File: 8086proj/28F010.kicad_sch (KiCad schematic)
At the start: 5 parts

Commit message: started sram
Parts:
- U3: value (none) -> 74LS138
- U4, U5, U6, U7: value (none) -> 28F010; footprint (none) -> 28F010
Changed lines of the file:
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@@
       (effects (font (size 1.27 1.27)) hide)
     )
-    (property "Value" "" (id 1) (at 204.47 85.09 0))
+    (property "Value" "GND" (id 1) (at 204.47 85.09 0))
     (property "Footprint" "" (id 2) (at 204.47 80.01 0)
       (effects (font (size 1.27 1.27)) hide)
@@
       (effects (font (size 1.27 1.27)) hide)
     )
-    (property "Value" "" (id 1) (at 265.43 109.22 0))
+    (property "Value" "+5V" (id 1) (at 265.43 109.22 0))
     (property "Footprint" "" (id 2) (at 265.43 114.3 0)
       (effects (font (size 1.27 1.27)) hide)
@@
       (effects (font (size 1.27 1.27)) hide)
     )
-    (property "Value" "" (id 1) (at 209.55 157.48 0))
+    (property "Value" "GND" (id 1) (at 209.55 157.48 0))
     (property "Footprint" "" (id 2) (at 209.55 152.4 0)
       (effects (font (size 1.27 1.27)) hide)
@@
       (effects (font (size 1.524 1.524)))
     )
-    (property "Value" "" (id 1) (at 161.29 35.56 0)
-      (effects (font (size 1.524 1.524)))
-    )
-    (property "Footprint" "" (id 2) (at 161.29 37.084 0)
+    (property "Value" "28F010" (id 1) (at 161.29 35.56 0)
+      (effects (font (size 1.524 1.524)))
+    )
+    (property "Footprint" "28F010" (id 2) (at 161.29 37.084 0)
       (effects (font (size 1.524 1.524)) hide)
     )
@@
       (effects (font (size 1.27 1.27)) hide)
     )
-    (property "Value" "" (id 1) (at 186.69 111.76 0))
+    (property "Value" "+5V" (id 1) (at 186.69 111.76 0))
     (property "Footprint" "" (id 2) (at 186.69 116.84 0)
       (effects (font (size 1.27 1.27)) hide)
@@
       (effects (font (size 1.27 1.27)) hide)
     )
-    (property "Value" "" (id 1) (at 265.43 36.83 0))
+    (property "Value" "+5V" (id 1) (at 265.43 36.83 0))
     (property "Footprint" "" (id 2) (at 265.43 41.91 0)
       (effects (font (size 1.27 1.27)) hide)
@@
       (effects (font (size 1.27 1.27)) hide)
     )
-    (property "Value" "" (id 1) (at 133.35 86.36 0))
+    (property "Value" "GND" (id 1) (at 133.35 86.36 0))
     (property "Footprint" "" (id 2) (at 133.35 81.28 0)
       (effects (font (size 1.27 1.27)) hide)
@@
       (effects (font (size 1.27 1.27)) hide)
     )
-    (property "Value" "" (id 1) (at 57.15 45.72 0)
+    (property "Value" "Earth" (id 1) (at 57.15 45.72 0)
       (effects (font (size 1.27 1.27)) hide)
     )
@@
     (in_bom yes) (on_board yes) (fields_autoplaced)
     (property "Reference" "U3" (id 0) (at 71.12 41.91 0))
-    (property "Value" "" (id 1) (at 71.12 44.45 0))
+    (property "Value" "74LS138" (id 1) (at 71.12 44.45 0))
     (property "Footprint" "" (id 2) (at 71.12 54.61 0)
       (effects (font (size 1.27 1.27)) hide)
@@
       (effects (font (size 1.27 1.27)) hide)
     )
-    (property "Value" "" (id 1) (at 130.81 160.02 0))
+    (property "Value" "GND" (id 1) (at 130.81 160.02 0))
     (property "Footprint" "" (id 2) (at 130.81 154.94 0)
       (effects (font (size 1.27 1.27)) hide)
@@
       (effects (font (size 1.524 1.524)))
     )
-    (property "Value" "" (id 1) (at 237.49 34.29 0)
-      (effects (font (size 1.524 1.524)))
-    )
-    (property "Footprint" "" (id 2) (at 237.49 35.814 0)
+    (property "Value" "28F010" (id 1) (at 237.49 34.29 0)
+      (effects (font (size 1.524 1.524)))
+    )
+    (property "Footprint" "28F010" (id 2) (at 237.49 35.814 0)
       (effects (font (size 1.524 1.524)) hide)
     )
@@
       (effects (font (size 1.27 1.27)) hide)
     )
-    (property "Value" "" (id 1) (at 189.23 38.1 0))
+    (property "Value" "+5V" (id 1) (at 189.23 38.1 0))
     (property "Footprint" "" (id 2) (at 189.23 43.18 0)
       (effects (font (size 1.27 1.27)) hide)
@@
       (effects (font (size 1.524 1.524)))
     )
-    (property "Value" "" (id 1) (at 237.49 106.68 0)
-      (effects (font (size 1.524 1.524)))
-    )
-    (property "Footprint" "" (id 2) (at 237.49 108.204 0)
+    (property "Value" "28F010" (id 1) (at 237.49 106.68 0)
+      (effects (font (size 1.524 1.524)))
+    )
+    (property "Footprint" "28F010" (id 2) (at 237.49 108.204 0)
       (effects (font (size 1.524 1.524)) hide)
     )
@@
       (effects (font (size 1.524 1.524)))
     )
-    (property "Value" "" (id 1) (at 158.75 109.22 0)
-      (effects (font (size 1.524 1.524)))
-    )
-    (property "Footprint" "" (id 2) (at 158.75 110.744 0)
+    (property "Value" "28F010" (id 1) (at 158.75 109.22 0)
+      (effects (font (size 1.524 1.524)))
+    )
+    (property "Footprint" "28F010" (id 2) (at 158.75 110.744 0)
       (effects (font (size 1.524 1.524)) hide)
     )

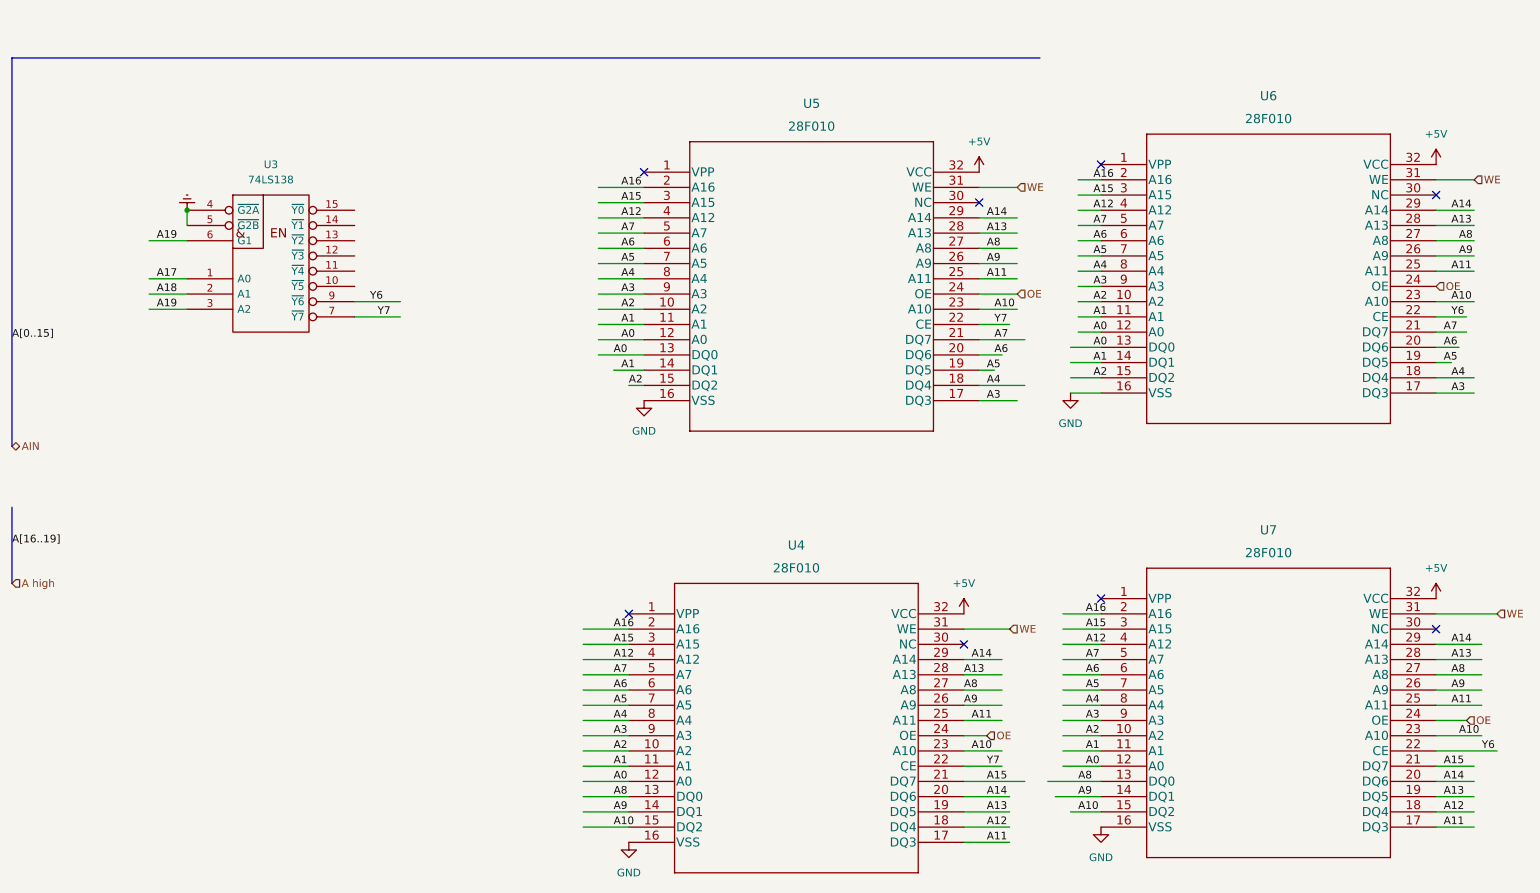
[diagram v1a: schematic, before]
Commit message: 28F010 fix
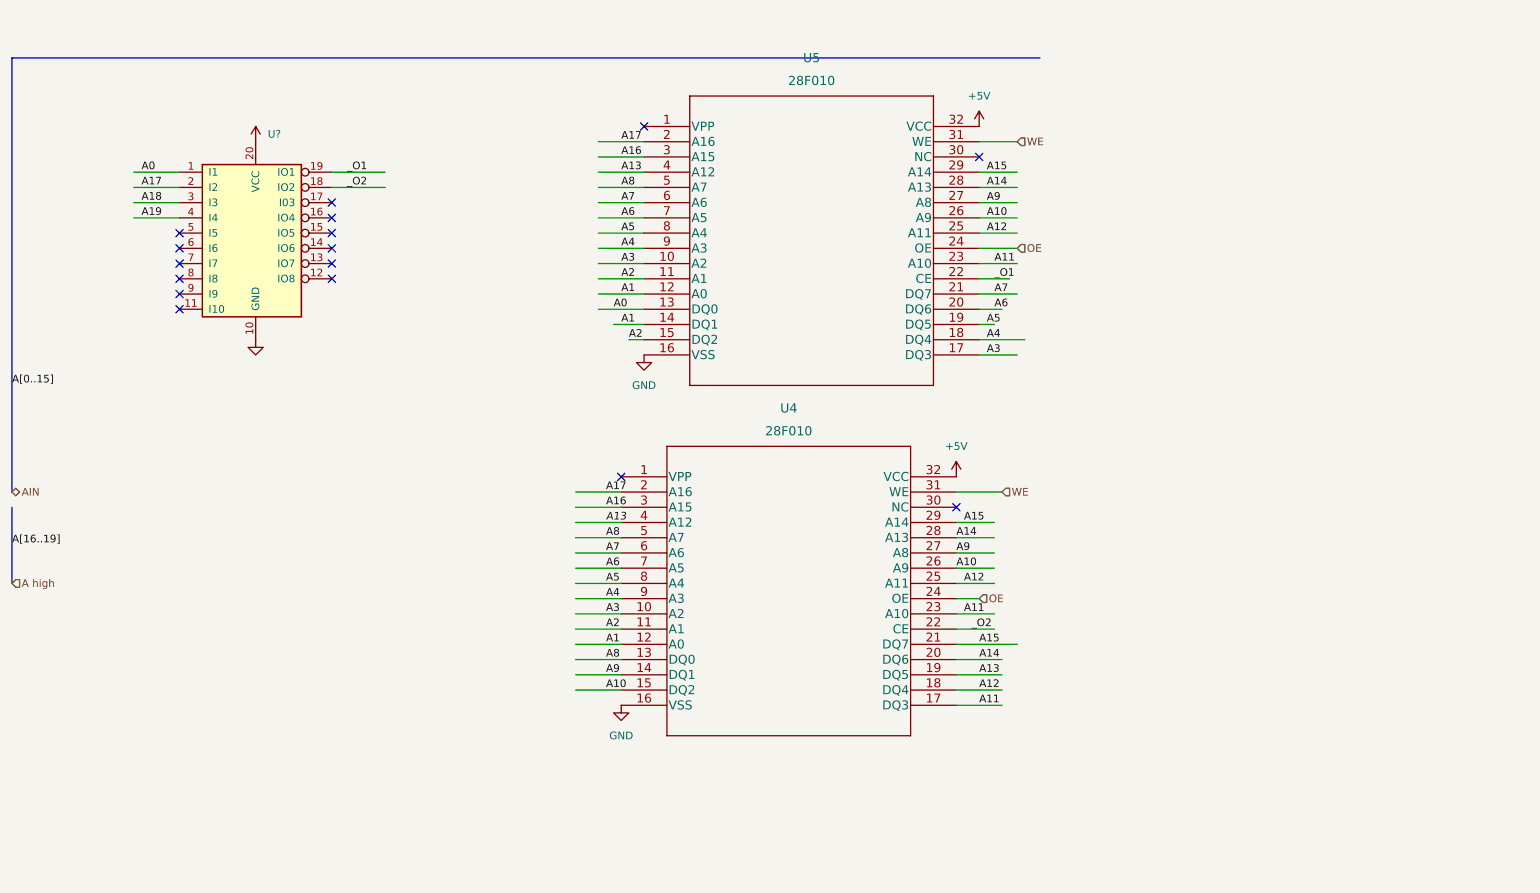
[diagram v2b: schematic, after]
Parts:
- removed U3: 74LS138, symbol 74xx_IEEE:74LS138
- removed U6, U7: 28F010, 28F010, symbol 28F010:28F010
- added U?: (no value), symbol Logic_Programmable:PAL16L8
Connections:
- net +5V: now also U?.20 (VCC)
- net A0: now also U?.1 (I1); no longer U4.12 (A0), U5.12 (A0)
- net A1: now also U4.12 (A0), U5.12 (A0); no longer U4.11 (A1), U5.11 (A1)
- net A10: now also U4.26 (A9), U5.26 (A9); no longer U4.23 (A10), U5.23 (A10)
- net A11: now also U4.23 (A10), U5.23 (A10); no longer U4.25 (A11), U5.25 (A11)
- net A12: now also U4.25 (A11), U5.25 (A11); no longer U4.4 (A12), U5.4 (A12)
- net A13: now also U4.4 (A12), U5.4 (A12); no longer U4.28 (A13), U5.28 (A13)
- net A14: now also U4.28 (A13), U5.28 (A13); no longer U4.29 (A14), U5.29 (A14)
- net A15: now also U4.29 (A14), U5.29 (A14); no longer U4.3 (A15), U5.3 (A15)
- net A16: now also U4.3 (A15), U5.3 (A15); no longer U4.2 (A16), U5.2 (A16)
- net A17: now also U4.2 (A16), U5.2 (A16), U?.2 (I2)
- net A18: now also U?.3 (I3)
- net A19: now also U?.4 (I4)
- net A2: now also U4.11 (A1), U5.11 (A1); no longer U4.10 (A2), U5.10 (A2)
- net A3: now also U4.10 (A2), U5.10 (A2); no longer U4.9 (A3), U5.9 (A3)
- net A4: now also U4.9 (A3), U5.9 (A3); no longer U4.8 (A4), U5.8 (A4)
- net A5: now also U4.8 (A4), U5.8 (A4); no longer U4.7 (A5), U5.7 (A5)
- net A6: now also U4.7 (A5), U5.7 (A5); no longer U4.6 (A6), U5.6 (A6)
- net A7: now also U4.6 (A6), U5.6 (A6); no longer U4.5 (A7), U5.5 (A7)
- net A8: now also U4.5 (A7), U5.5 (A7); no longer U4.27 (A8), U5.27 (A8)
- net A9: now also U4.27 (A8), U5.27 (A8); no longer U4.26 (A9), U5.26 (A9)
- net GND: now also U?.10 (GND)
- net Y7 renamed _O1
- net _O1: now also U?.19 (IO1); no longer U4.22 (CE)
- new net _O2: U4.22 (CE), U?.18 (IO2)
- no-connect marks 8 -> 16
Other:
- moved on the sheet: U4, U5

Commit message: latch added
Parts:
- U?: value (none) -> PAL16L8
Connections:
- net A0: no longer U5.13 (DQ0)
- net A1: no longer U5.14 (DQ1)
- net A10: no longer U4.15 (DQ2)
- net A11: no longer U4.17 (DQ3)
- net A12: no longer U4.18 (DQ4)
- net A13: no longer U4.19 (DQ5)
- net A14: no longer U4.20 (DQ6)
- net A15: no longer U4.21 (DQ7)
- net A2: no longer U5.15 (DQ2)
- net A3: no longer U5.17 (DQ3)
- net A4: no longer U5.18 (DQ4)
- net A5: no longer U5.19 (DQ5)
- net A6: no longer U5.20 (DQ6)
- net A7: no longer U5.21 (DQ7)
- net A8: no longer U4.13 (DQ0)
- net A9: no longer U4.14 (DQ1)
- new net D0: U5.13 (DQ0)
- new net D1: U5.14 (DQ1)
- new net D10: U4.15 (DQ2)
- new net D11: U4.17 (DQ3)
- new net D12: U4.18 (DQ4)
- new net D13: U4.19 (DQ5)
- new net D14: U4.20 (DQ6)
- new net D15: U4.21 (DQ7)
- new net D2: U5.15 (DQ2)
- new net D3: U5.17 (DQ3)
- new net D4: U5.18 (DQ4)
- new net D5: U5.19 (DQ5)
- new net D6: U5.20 (DQ6)
- new net D7: U5.21 (DQ7)
- new net D8: U4.13 (DQ0)
- new net D9: U4.14 (DQ1)
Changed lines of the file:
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@@
-    (stroke (width 0) (type default) (color 0 0 0 0))
-  )
-  (bus (pts (xy 27.94 99.06) (xy 27.94 111.76))
     (stroke (width 0) (type default) (color 0 0 0 0))
   )
@@
     (stroke (width 0) (type default) (color 0 0 0 0))
   )
+  (bus (pts (xy 27.94 109.22) (xy 27.94 130.81))
+    (stroke (width 0) (type default) (color 0 0 0 0))
+  )
   (wire (pts (xy 189.23 68.58) (xy 191.77 68.58))
     (stroke (width 0) (type default) (color 0 0 0 0))
@@
     (effects (font (size 1.27 1.27)) (justify left bottom))
   )
-  (label "A0" (at 128.27 66.04 0)
-    (effects (font (size 1.27 1.27)) (justify left bottom))
-  )
-  (label "A7" (at 191.77 63.5 0)
-    (effects (font (size 1.27 1.27)) (justify left bottom))
-  )
-  (label "A13" (at 189.23 127 0)
+  (label "D0" (at 128.27 66.04 0)
+    (effects (font (size 1.27 1.27)) (justify left bottom))
+  )
+  (label "D7" (at 191.77 63.5 0)
+    (effects (font (size 1.27 1.27)) (justify left bottom))
+  )
+  (label "D13" (at 189.23 127 0)
     (effects (font (size 1.27 1.27)) (justify left bottom))
   )
@@
     (effects (font (size 1.27 1.27)) (justify left bottom))
   )
-  (label "A2" (at 130.81 71.12 0)
-    (effects (font (size 1.27 1.27)) (justify left bottom))
-  )
-  (label "A5" (at 190.5 68.58 0)
+  (label "D2" (at 130.81 71.12 0)
+    (effects (font (size 1.27 1.27)) (justify left bottom))
+  )
+  (label "D5" (at 190.5 68.58 0)
     (effects (font (size 1.27 1.27)) (justify left bottom))
   )
@@
     (effects (font (size 1.27 1.27)) (justify left bottom))
   )
-  (label "A6" (at 191.77 66.04 0)
+  (label "D6" (at 191.77 66.04 0)
     (effects (font (size 1.27 1.27)) (justify left bottom))
   )
@@
     (effects (font (size 1.27 1.27)) (justify left bottom))
   )
-  (label "A9" (at 127 127 0)
-    (effects (font (size 1.27 1.27)) (justify left bottom))
-  )
-  (label "A1" (at 129.54 68.58 0)
+  (label "D9" (at 127 127 0)
+    (effects (font (size 1.27 1.27)) (justify left bottom))
+  )
+  (label "D1" (at 129.54 68.58 0)
     (effects (font (size 1.27 1.27)) (justify left bottom))
   )
@@
     (effects (font (size 1.27 1.27)) (justify left bottom))
   )
-  (label "A8" (at 127 124.46 0)
+  (label "D8" (at 127 124.46 0)
+    (effects (font (size 1.27 1.27)) (justify left bottom))
+  )
+  (label "D[0..15]" (at 27.94 119.38 0)
     (effects (font (size 1.27 1.27)) (justify left bottom))
   )
@@
     (effects (font (size 1.27 1.27)) (justify left bottom))
   )
-  (label "A10" (at 127 129.54 0)
+  (label "D10" (at 127 129.54 0)
     (effects (font (size 1.27 1.27)) (justify left bottom))
   )
@@
     (effects (font (size 1.27 1.27)) (justify left bottom))
   )
-  (label "A15" (at 189.23 121.92 0)
-    (effects (font (size 1.27 1.27)) (justify left bottom))
-  )
-  (label "A11" (at 189.23 132.08 0)
+  (label "D15" (at 189.23 121.92 0)
+    (effects (font (size 1.27 1.27)) (justify left bottom))
+  )
+  (label "D11" (at 189.23 132.08 0)
     (effects (font (size 1.27 1.27)) (justify left bottom))
   )
@@
     (effects (font (size 1.27 1.27)) (justify left bottom))
   )
-  (label "A[0..15]" (at 27.94 78.74 0)
+  (label "A[0..19]" (at 27.94 78.74 0)
     (effects (font (size 1.27 1.27)) (justify left bottom))
   )
@@
     (effects (font (size 1.27 1.27)) (justify left bottom))
   )
-  (label "A14" (at 189.23 124.46 0)
+  (label "D14" (at 189.23 124.46 0)
     (effects (font (size 1.27 1.27)) (justify left bottom))
   )
@@
     (effects (font (size 1.27 1.27)) (justify left bottom))
   )
-  (label "A4" (at 190.5 71.12 0)
+  (label "D4" (at 190.5 71.12 0)
     (effects (font (size 1.27 1.27)) (justify left bottom))
   )
@@
     (effects (font (size 1.27 1.27)) (justify left bottom))
   )
-  (label "A[16..19]" (at 27.94 105.41 0)
-    (effects (font (size 1.27 1.27)) (justify left bottom))
-  )
-  (label "A3" (at 190.5 73.66 0)
+  (label "D3" (at 190.5 73.66 0)
     (effects (font (size 1.27 1.27)) (justify left bottom))
   )
@@
     (effects (font (size 1.27 1.27)) (justify left bottom))
   )
-  (label "A12" (at 189.23 129.54 0)
+  (label "D12" (at 189.23 129.54 0)
     (effects (font (size 1.27 1.27)) (justify left bottom))
   )
@@
     (effects (font (size 1.27 1.27)) (justify left))
   )
+  (hierarchical_label "DATA" (shape bidirectional) (at 27.94 130.81 0)
+    (effects (font (size 1.27 1.27)) (justify left))
+  )
   (hierarchical_label "WE" (shape input) (at 193.04 96.52 0)
     (effects (font (size 1.27 1.27)) (justify left))
   )
-  (hierarchical_label "A high" (shape input) (at 27.94 111.76 0)
-    (effects (font (size 1.27 1.27)) (justify left))
-  )
-  (hierarchical_label "AIN" (shape bidirectional) (at 27.94 96.52 0)
+  (hierarchical_label "AIN" (shape input) (at 27.94 96.52 0)
     (effects (font (size 1.27 1.27)) (justify left))
   )
@@
       (effects (font (size 1.27 1.27)) (justify left))
     )
-    (property "Value" "" (id 1) (at 70.5994 39.37 0)
+    (property "Value" "PAL16L8" (id 1) (at 70.5994 39.37 0)
       (effects (font (size 1.27 1.27)) (justify left))
     )
@@
       (effects (font (size 1.27 1.27)) hide)
     )
-    (property "Value" "" (id 1) (at 68.58 76.2 0))
+    (property "Value" "GND" (id 1) (at 68.58 76.2 0))
     (property "Footprint" "" (id 2) (at 68.58 71.12 0)
       (effects (font (size 1.27 1.27)) hide)
@@
       (effects (font (size 1.27 1.27)) hide)
     )
-    (property "Value" "" (id 1) (at 68.58 33.02 0))
+    (property "Value" "+5V" (id 1) (at 68.58 33.02 0))
     (property "Footprint" "" (id 2) (at 68.58 38.1 0)
       (effects (font (size 1.27 1.27)) hide)
